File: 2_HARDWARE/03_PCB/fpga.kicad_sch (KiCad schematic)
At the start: 23 parts, among them U12 ICE40UP5K-SG48ITR

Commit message: MINOR: Changed Boot Select Switches to Pull-Downs / Pull Up DNI and continued layout.
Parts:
- renumbered R34 to R35, R35 to R36, R36 to R37, R37 to R38, R38 to R39, R39 to R40, R40 to R41

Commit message: MINOR: Added Power and GND Vias on the Top Layer.
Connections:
- no-connect marks 13 -> 14
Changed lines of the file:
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@@
+	)
+	(no_connect
+		(at 92.71 62.23)
 	)
 	(no_connect

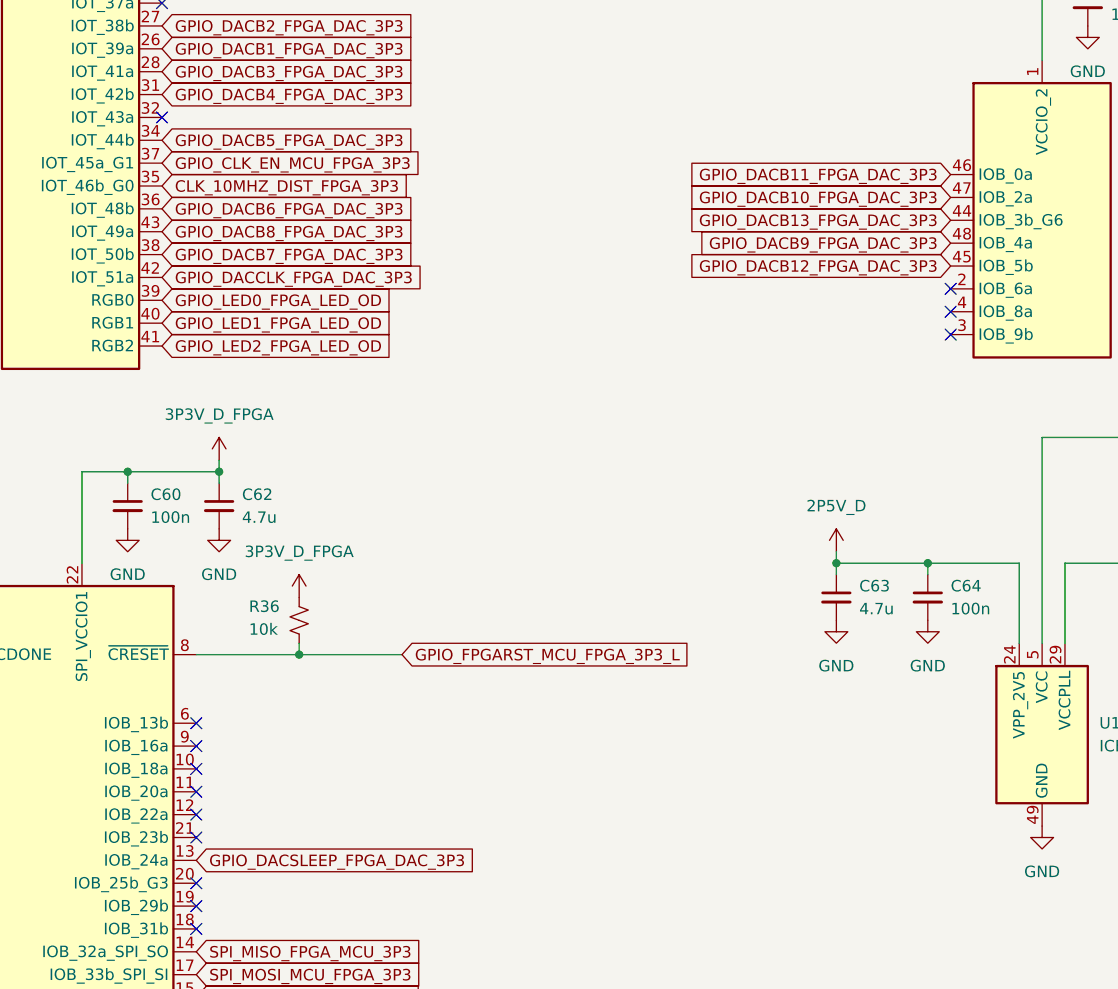
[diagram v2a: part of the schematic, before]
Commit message: FEAT: Routed FPGA to DDS and FPGA to MCU Signals.
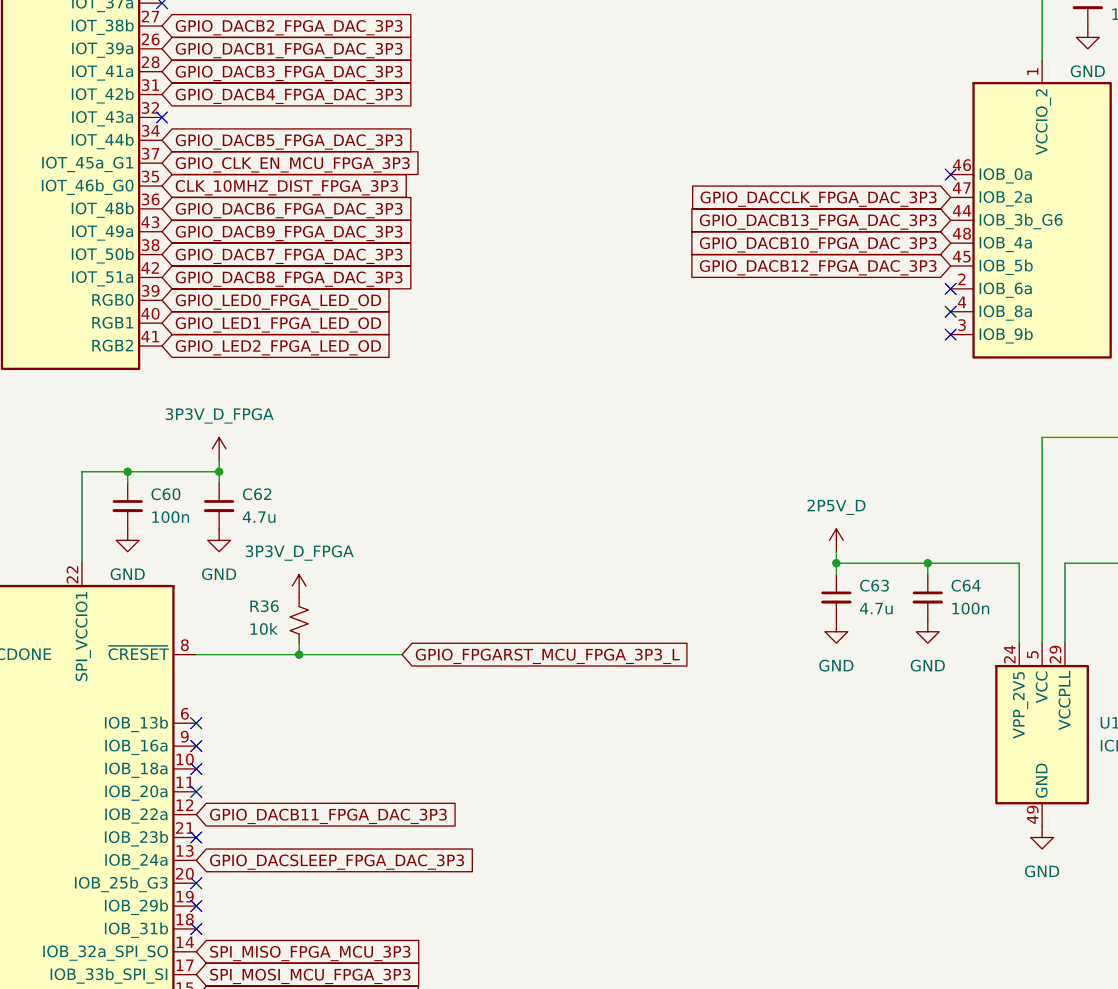
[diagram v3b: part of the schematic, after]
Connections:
- net GPIO_DACB10_FPGA_DAC_3P3: now also U12.48 (IOB_4a); no longer U12.47 (IOB_2a)
- net GPIO_DACB11_FPGA_DAC_3P3: now also U12.12 (IOB_22a); no longer U12.46 (IOB_0a)
- net GPIO_DACB8_FPGA_DAC_3P3: now also U12.42 (IOT_51a); no longer U12.43 (IOT_49a)
- net GPIO_DACB9_FPGA_DAC_3P3: now also U12.43 (IOT_49a); no longer U12.48 (IOB_4a)
- net GPIO_DACCLK_FPGA_DAC_3P3: now also U12.47 (IOB_2a); no longer U12.42 (IOT_51a)
